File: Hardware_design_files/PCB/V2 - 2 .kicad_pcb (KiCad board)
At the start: 2 copper layers, 168 x 123 mm, 131 parts, among them CON1 BARREL_JACK, P1 CONN_01X02, Q1 TIP120, SW1 SPST

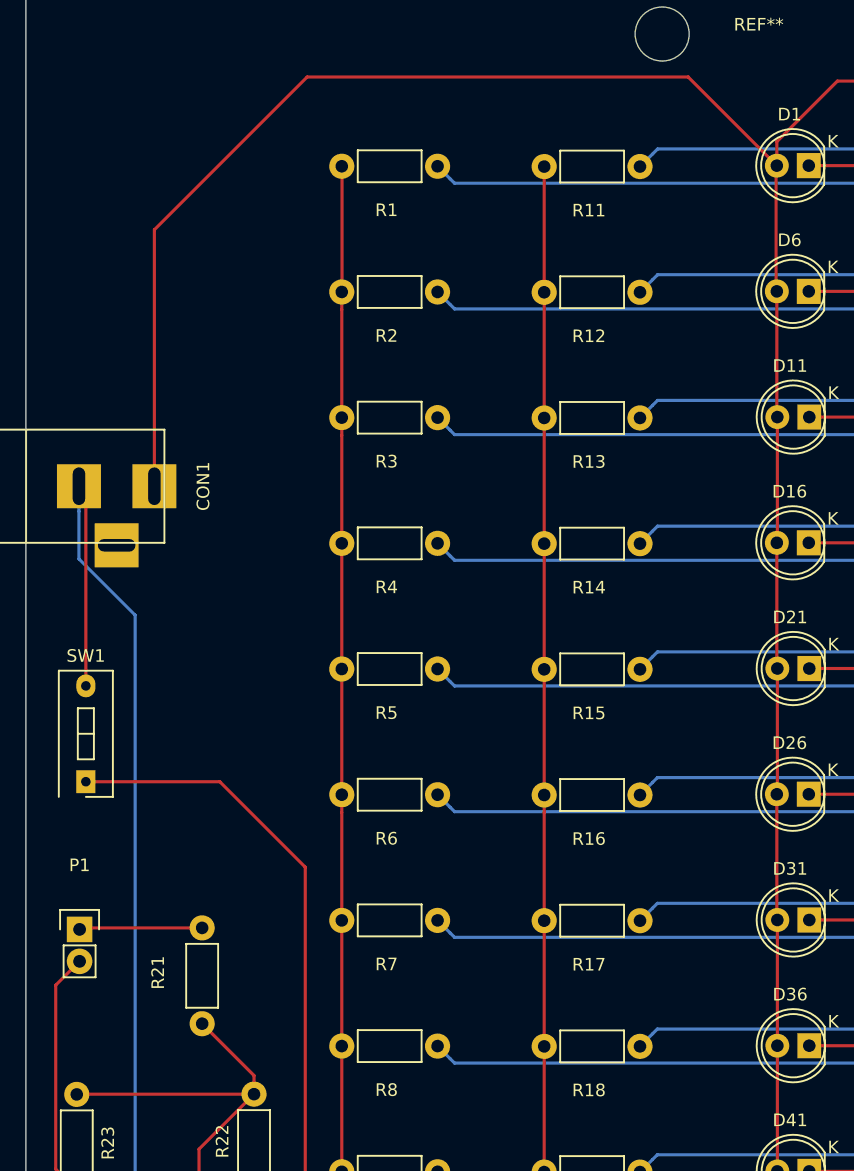
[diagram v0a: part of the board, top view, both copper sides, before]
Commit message: moved positive track away from screw hole, so that the screw does not damage it when placed in
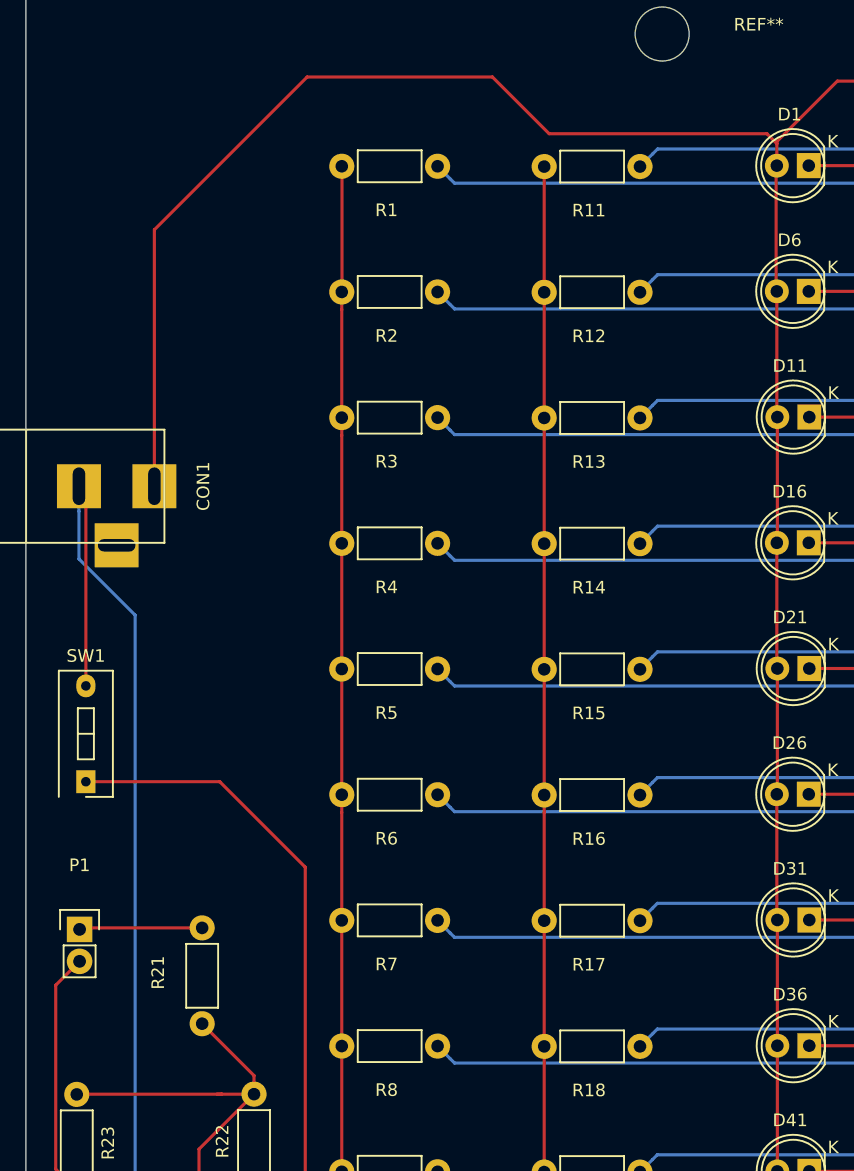
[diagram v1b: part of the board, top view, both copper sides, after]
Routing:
- net Net-(CON1-Pad1): track 314.8 -> 314.1 mm
